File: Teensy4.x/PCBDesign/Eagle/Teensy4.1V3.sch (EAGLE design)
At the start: 8 parts

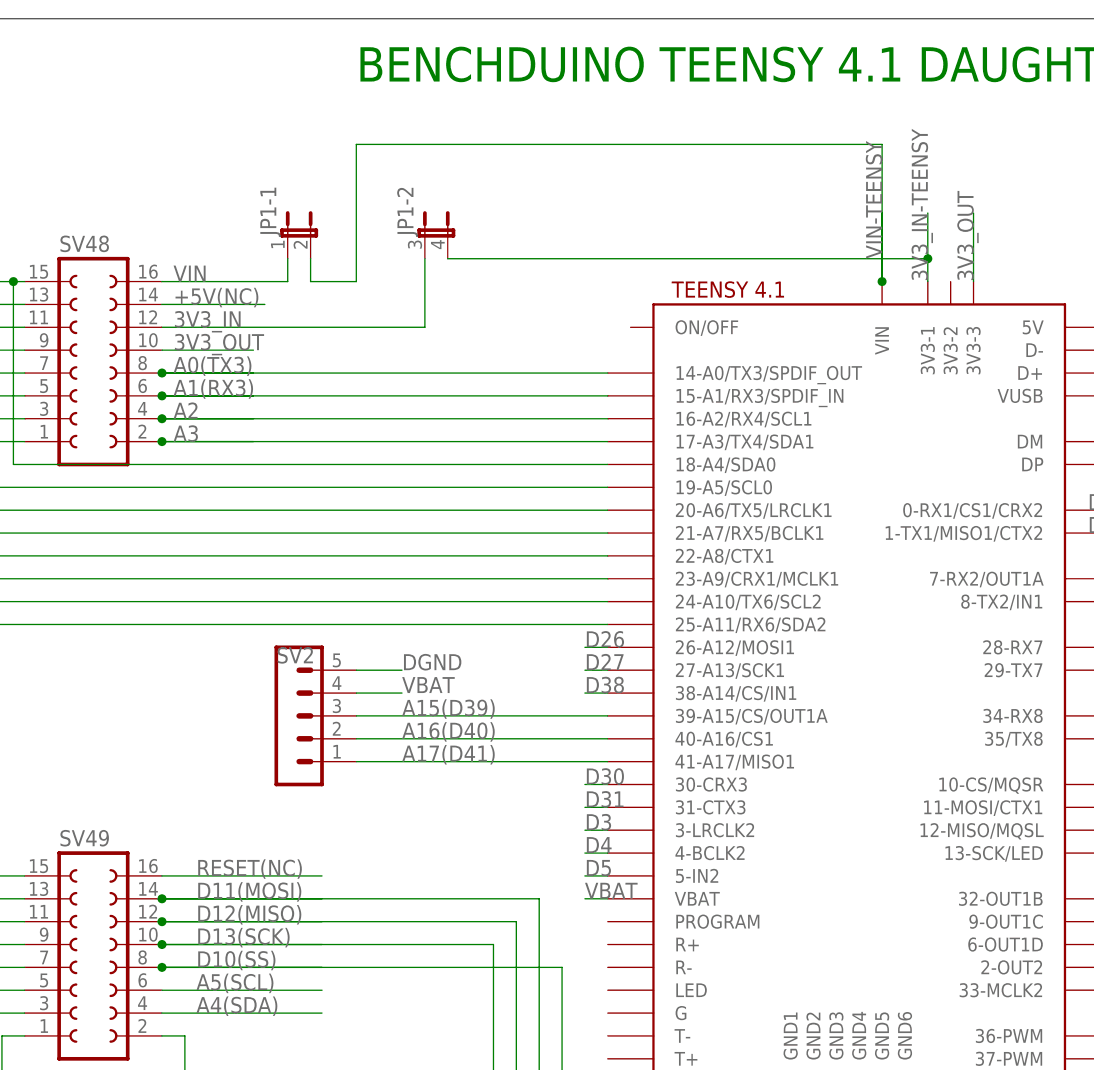
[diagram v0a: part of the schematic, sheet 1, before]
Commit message: Updated Teensy to correct power error
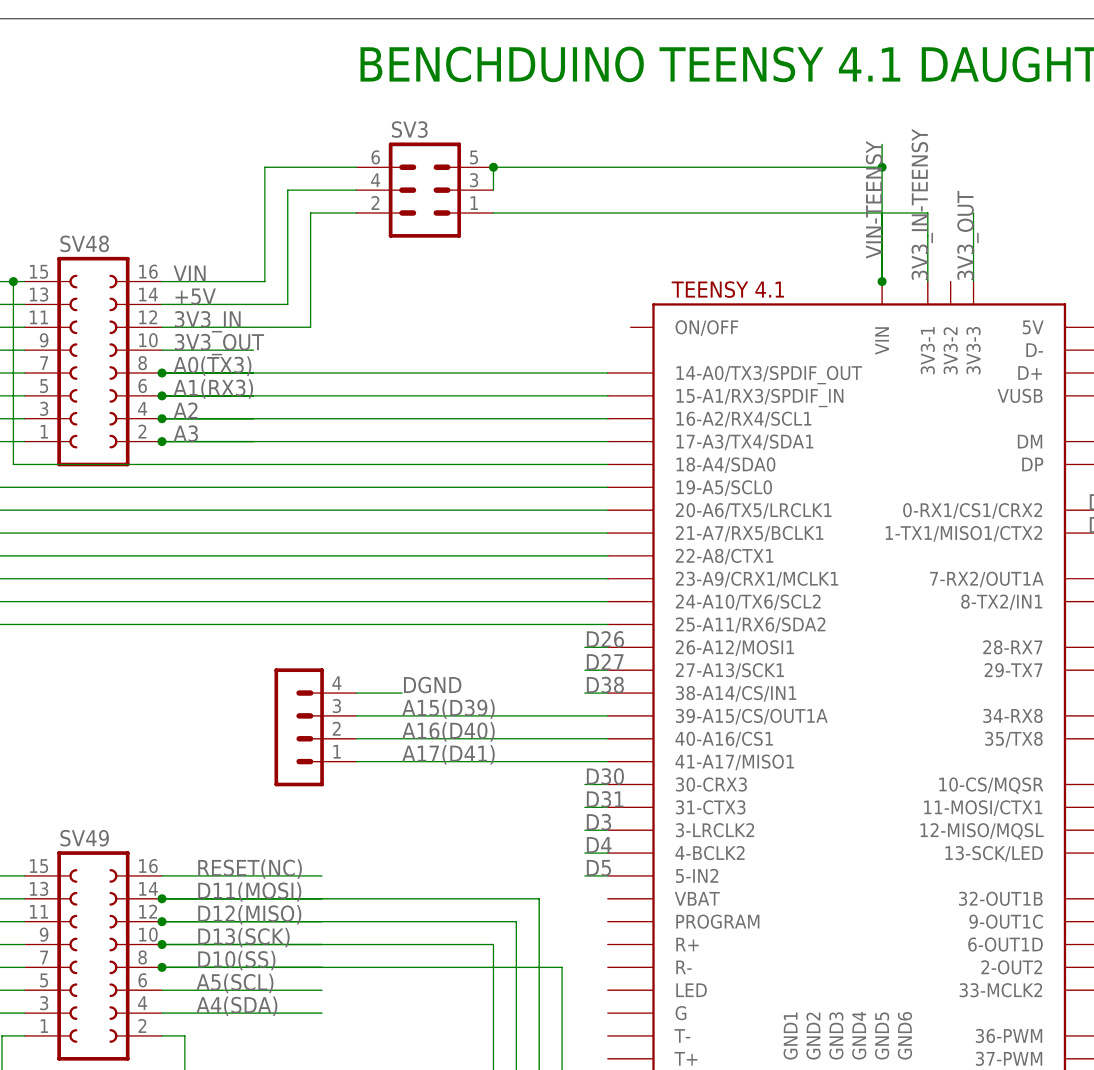
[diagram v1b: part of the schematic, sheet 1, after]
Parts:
- removed JP1: (no value), jumper:JP2QE
- removed SV2: (no value), con-lstb:MA05-1
- added SV3: (no value), con-lstb:MA03-2
- added SV4: (no value), con-lstb:MA04-1
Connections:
- removed net +5V(NC): SV48.14
- removed net VBAT: SV2.4, U$1.VBAT
- new net +5V: SV3.4, SV48.14
- net 3V3_IN: now also SV3.2; no longer JP1-2.1
- net 3V3_IN-TEENSY: now also SV3.1; no longer JP1-2.2
- net A15(D39): now also SV4.3; no longer SV2.3
- net A16(D40): now also SV4.2; no longer SV2.2
- net A17(D41): now also SV4.1; no longer SV2.1
- net DGND: now also SV4.4; no longer SV2.5
- net VIN: now also SV3.6; no longer JP1-1.1
- net VIN-TEENSY: now also SV3.3, SV3.5; no longer JP1-1.2
